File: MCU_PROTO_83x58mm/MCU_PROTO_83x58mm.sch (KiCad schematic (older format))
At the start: 15 parts, among them J1 Screw_Terminal_01x03, J10 Conn_01x01_Male, J2 Screw_Terminal_01x03, J3 Conn_01x20_Female, J4 Conn_01x20_Female, J5 Conn_01x20_Female, J6 Conn_01x20_Female, J7 Conn_01x20_Female, J8 Conn_01x20_Female, J9 Conn_01x01_Male

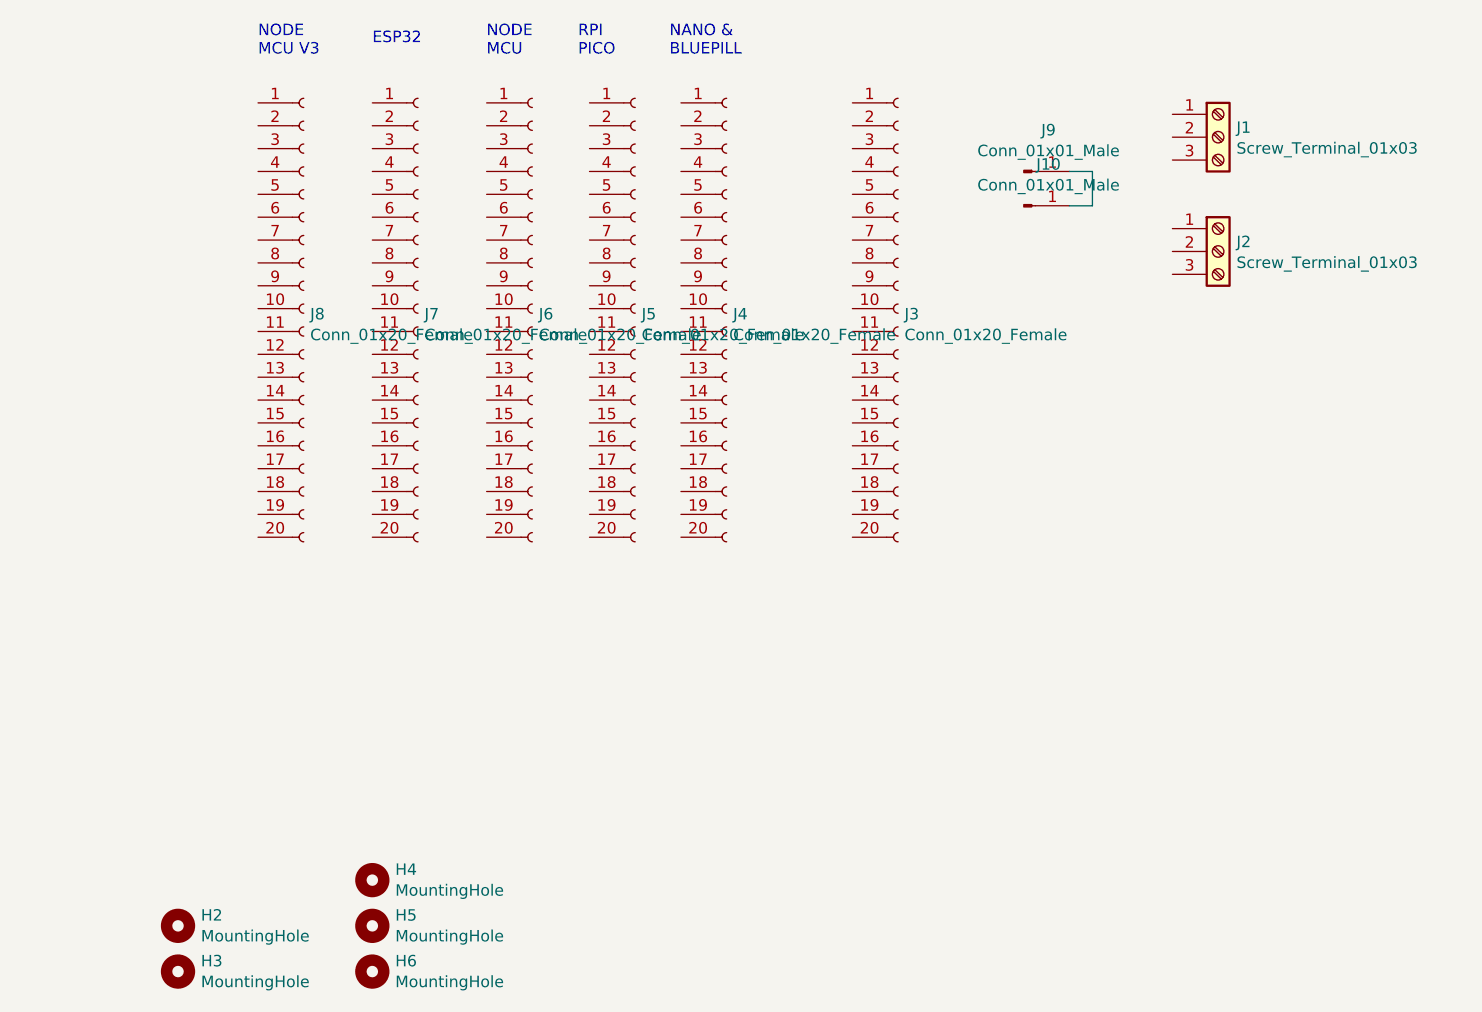
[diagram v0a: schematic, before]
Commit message: added rpi zero compat started
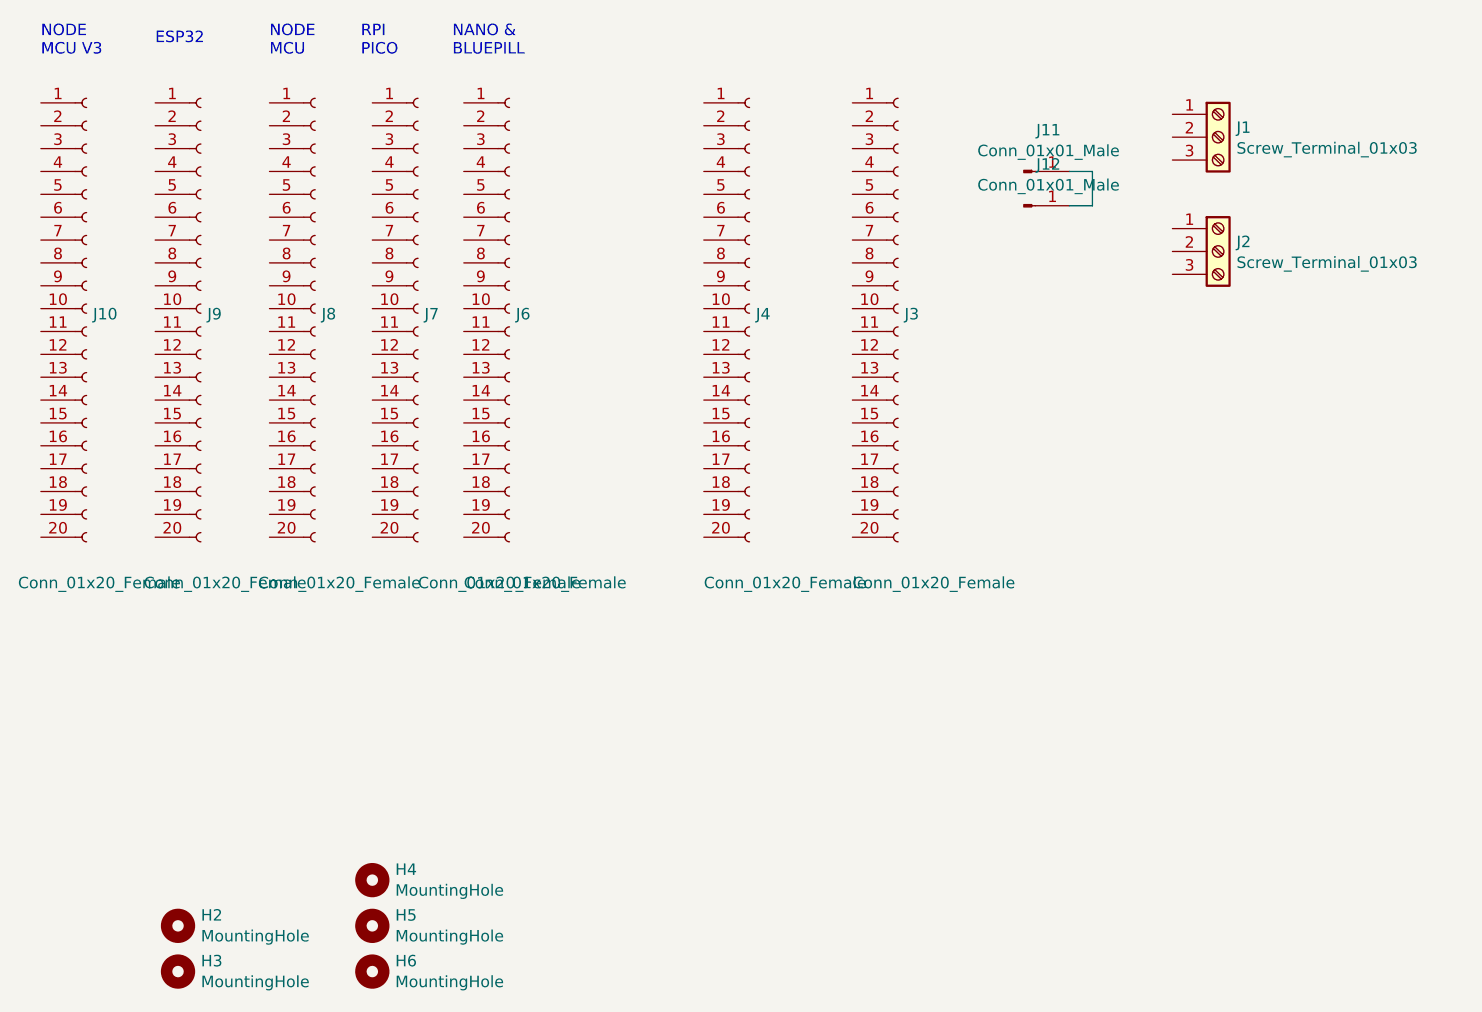
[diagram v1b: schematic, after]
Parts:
- added J4: Conn_01x20_Female, Connector_PinSocket_2.54mm:PinSocket_1x20_P2.54mm_Vertical, symbol Connector:Conn_01x20_Female
- renumbered J8 to J10, J9 to J11, J10 to J12, J4 to J6, J5 to J7, J6 to J8, J7 to J9
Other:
- moved on the sheet: J10, J6, J7, J8, J9
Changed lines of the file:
@@
 $EndComp
 $Comp
-L Connector:Conn_01x01_Male J9
+L Connector:Conn_01x01_Male J11
 U 1 1 6192FB40
 P 7300 1950
-F 0 "J9" H 7408 2131 50  0000 C CNN
+F 0 "J11" H 7408 2131 50  0000 C CNN
 F 1 "Conn_01x01_Male" H 7408 2040 50  0000 C CNN
 F 2 "Connector_Wire:SolderWirePad_1x01_Drill0.8mm" H 7300 1950 50  0001 C CNN
@@
 $EndComp
 $Comp
-L Connector:Conn_01x01_Male J10
+L Connector:Conn_01x01_Male J12
 U 1 1 61938D6F
 P 7300 2100
-F 0 "J10" H 7408 2281 50  0000 C CNN
+F 0 "J12" H 7408 2281 50  0000 C CNN
 F 1 "Conn_01x01_Male" H 7408 2190 50  0000 C CNN
 F 2 "Connector_Wire:SolderWirePad_1x01_Drill0.8mm" H 7300 2100 50  0001 C CNN
@@
 	7600 2100 7500 2100
 $Comp
-L Connector:Conn_01x20_Female J5
+L Connector:Conn_01x20_Female J7
 U 1 1 619361D7
-P 5600 2550
-F 0 "J5" H 5628 2526 50  0000 L CNN
-F 1 "Conn_01x20_Female" H 5628 2435 50  0000 L CNN
-F 2 "Connector_PinSocket_2.54mm:PinSocket_1x20_P2.54mm_Vertical" H 5600 2550 50  0001 C CNN
-F 3 "~" H 5600 2550 50  0001 C CNN
-	1    5600 2550
+P 4650 2550
+F 0 "J7" H 4678 2526 50  0000 L CNN
+F 1 "Conn_01x20_Female" H 4650 1350 50  0000 L CNN
+F 2 "Connector_PinSocket_2.54mm:PinSocket_1x20_P2.54mm_Vertical" H 4650 2550 50  0001 C CNN
+F 3 "~" H 4650 2550 50  0001 C CNN
+	1    4650 2550
 	1    0    0    -1
 $EndComp
@@
 P 6750 2550
 F 0 "J3" H 6778 2526 50  0000 L CNN
-F 1 "Conn_01x20_Female" H 6778 2435 50  0000 L CNN
+F 1 "Conn_01x20_Female" H 6550 1350 50  0000 L CNN
 F 2 "Connector_PinSocket_2.54mm:PinSocket_1x20_P2.54mm_Vertical" H 6750 2550 50  0001 C CNN
 F 3 "~" H 6750 2550 50  0001 C CNN
@@
 	1    0    0    -1
 $EndComp
-Text Notes 5750 1450 0    50   ~ 0
+Text Notes 4800 1450 0    50   ~ 0
 NANO &\nBLUEPILL
 $Comp
-L Connector:Conn_01x20_Female J4
+L Connector:Conn_01x20_Female J6
 U 1 1 61975404
-P 6000 2550
-F 0 "J4" H 6028 2526 50  0000 L CNN
-F 1 "Conn_01x20_Female" H 6028 2435 50  0000 L CNN
-F 2 "Connector_PinSocket_2.54mm:PinSocket_1x20_P2.54mm_Vertical" H 6000 2550 50  0001 C CNN
-F 3 "~" H 6000 2550 50  0001 C CNN
-	1    6000 2550
+P 5050 2550
+F 0 "J6" H 5078 2526 50  0000 L CNN
+F 1 "Conn_01x20_Female" H 4850 1350 50  0000 L CNN
+F 2 "Connector_PinSocket_2.54mm:PinSocket_1x20_P2.54mm_Vertical" H 5050 2550 50  0001 C CNN
+F 3 "~" H 5050 2550 50  0001 C CNN
+	1    5050 2550
 	1    0    0    -1
 $EndComp
-Text Notes 5350 1450 0    50   ~ 0
+Text Notes 4400 1450 0    50   ~ 0
 RPI\nPICO
 $Comp
-L Connector:Conn_01x20_Female J6
+L Connector:Conn_01x20_Female J8
 U 1 1 6199B975
-P 5150 2550
-F 0 "J6" H 5178 2526 50  0000 L CNN
-F 1 "Conn_01x20_Female" H 5178 2435 50  0000 L CNN
-F 2 "Connector_PinSocket_2.54mm:PinSocket_1x20_P2.54mm_Vertical" H 5150 2550 50  0001 C CNN
-F 3 "~" H 5150 2550 50  0001 C CNN
-	1    5150 2550
+P 4200 2550
+F 0 "J8" H 4228 2526 50  0000 L CNN
+F 1 "Conn_01x20_Female" H 3950 1350 50  0000 L CNN
+F 2 "Connector_PinSocket_2.54mm:PinSocket_1x20_P2.54mm_Vertical" H 4200 2550 50  0001 C CNN
+F 3 "~" H 4200 2550 50  0001 C CNN
+	1    4200 2550
 	1    0    0    -1
 $EndComp
-Text Notes 4950 1450 0    50   ~ 0
+Text Notes 4000 1450 0    50   ~ 0
 NODE\nMCU
 $Comp
-L Connector:Conn_01x20_Female J7
+L Connector:Conn_01x20_Female J9
 U 1 1 619B2BAA
-P 4650 2550
-F 0 "J7" H 4678 2526 50  0000 L CNN
-F 1 "Conn_01x20_Female" H 4678 2435 50  0000 L CNN
-F 2 "Connector_PinSocket_2.54mm:PinSocket_1x20_P2.54mm_Vertical" H 4650 2550 50  0001 C CNN
-F 3 "~" H 4650 2550 50  0001 C CNN
-	1    4650 2550
+P 3700 2550
+F 0 "J9" H 3728 2526 50  0000 L CNN
+F 1 "Conn_01x20_Female" H 3450 1350 50  0000 L CNN
+F 2 "Connector_PinSocket_2.54mm:PinSocket_1x20_P2.54mm_Vertical" H 3700 2550 50  0001 C CNN
+F 3 "~" H 3700 2550 50  0001 C CNN
+	1    3700 2550
 	1    0    0    -1
 $EndComp
-Text Notes 4450 1400 0    50   ~ 0
+Text Notes 3500 1400 0    50   ~ 0
 ESP32
 $Comp
-L Connector:Conn_01x20_Female J8
+L Connector:Conn_01x20_Female J10
 U 1 1 619DA776
-P 4150 2550
-F 0 "J8" H 4178 2526 50  0000 L CNN
-F 1 "Conn_01x20_Female" H 4178 2435 50  0000 L CNN
-F 2 "Connector_PinSocket_2.54mm:PinSocket_1x20_P2.54mm_Vertical" H 4150 2550 50  0001 C CNN
-F 3 "~" H 4150 2550 50  0001 C CNN
-	1    4150 2550
+P 3200 2550
+F 0 "J10" H 3228 2526 50  0000 L CNN
+F 1 "Conn_01x20_Female" H 2900 1350 50  0000 L CNN
+F 2 "Connector_PinSocket_2.54mm:PinSocket_1x20_P2.54mm_Vertical" H 3200 2550 50  0001 C CNN
+F 3 "~" H 3200 2550 50  0001 C CNN
+	1    3200 2550
 	1    0    0    -1
 $EndComp
-Text Notes 3950 1450 0    50   ~ 0
+Text Notes 3000 1450 0    50   ~ 0
 NODE\nMCU V3
 $Comp
@@
 	1    0    0    -1
 $EndComp
+$Comp
+L Connector:Conn_01x20_Female J4
+U 1 1 6217E1D9
+P 6100 2550
+F 0 "J4" H 6128 2526 50  0000 L CNN
+F 1 "Conn_01x20_Female" H 5900 1350 50  0000 L CNN
+F 2 "Connector_PinSocket_2.54mm:PinSocket_1x20_P2.54mm_Vertical" H 6100 2550 50  0001 C CNN
+F 3 "~" H 6100 2550 50  0001 C CNN
+	1    6100 2550
+	1    0    0    -1
+$EndComp

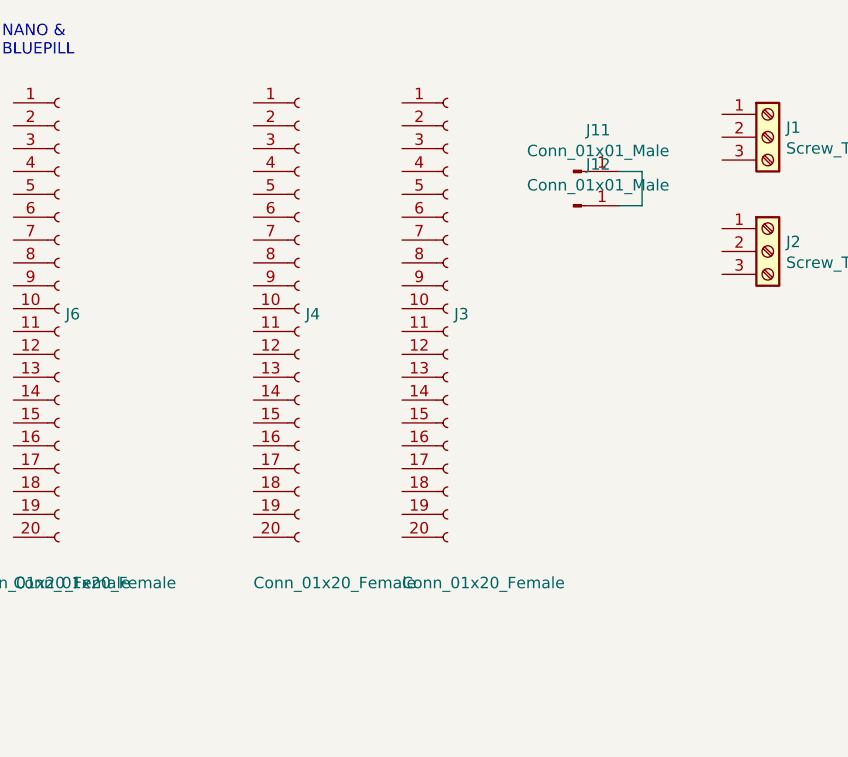
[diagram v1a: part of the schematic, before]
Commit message: pi zero added single gerber
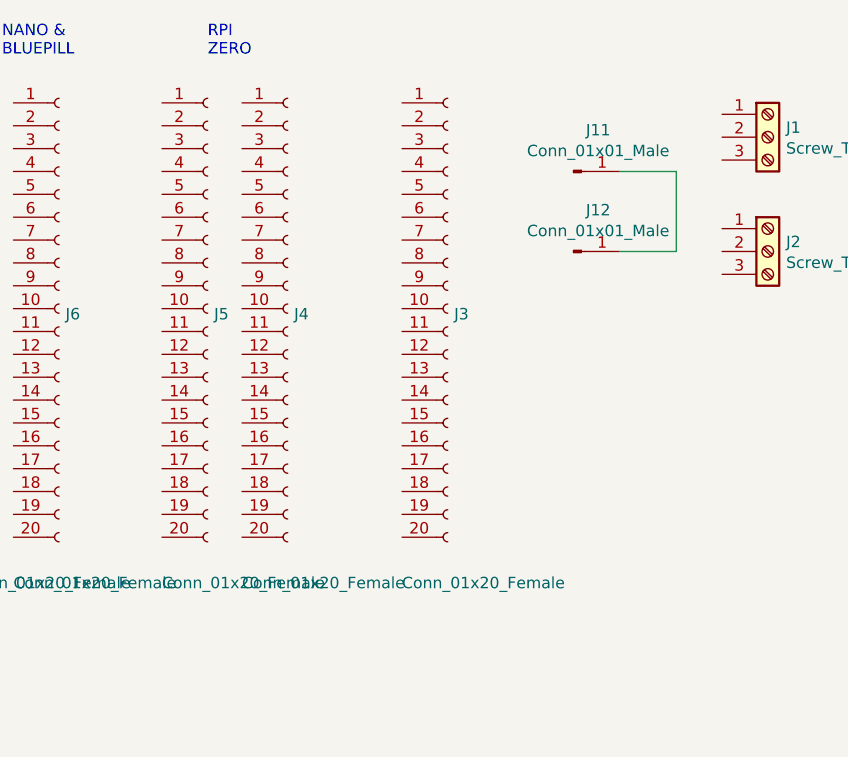
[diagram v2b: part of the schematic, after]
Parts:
- added J5: Conn_01x20_Female, Connector_PinSocket_2.54mm:PinSocket_1x20_P2.54mm_Vertical, symbol Connector:Conn_01x20_Female
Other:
- note added: "RPI\nZERO"
- moved on the sheet: J12, J4
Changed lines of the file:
@@
 L Connector:Conn_01x01_Male J12
 U 1 1 61938D6F
-P 7300 2100
-F 0 "J12" H 7408 2281 50  0000 C CNN
-F 1 "Conn_01x01_Male" H 7408 2190 50  0000 C CNN
-F 2 "Connector_Wire:SolderWirePad_1x01_Drill0.8mm" H 7300 2100 50  0001 C CNN
-F 3 "~" H 7300 2100 50  0001 C CNN
-	1    7300 2100
+P 7300 2300
+F 0 "J12" H 7408 2481 50  0000 C CNN
+F 1 "Conn_01x01_Male" H 7408 2390 50  0000 C CNN
+F 2 "Connector_Wire:SolderWirePad_1x01_Drill0.8mm" H 7300 2300 50  0001 C CNN
+F 3 "~" H 7300 2300 50  0001 C CNN
+	1    7300 2300
 	1    0    0    -1
 $EndComp
-Wire Wire Line
-	7500 1950 7600 1950
-Wire Wire Line
-	7600 1950 7600 2100
-Wire Wire Line
-	7600 2100 7500 2100
 $Comp
 L Connector:Conn_01x20_Female J7
@@
 L Connector:Conn_01x20_Female J4
 U 1 1 6217E1D9
-P 6100 2550
-F 0 "J4" H 6128 2526 50  0000 L CNN
-F 1 "Conn_01x20_Female" H 5900 1350 50  0000 L CNN
-F 2 "Connector_PinSocket_2.54mm:PinSocket_1x20_P2.54mm_Vertical" H 6100 2550 50  0001 C CNN
-F 3 "~" H 6100 2550 50  0001 C CNN
-	1    6100 2550
+P 6050 2550
+F 0 "J4" H 6078 2526 50  0000 L CNN
+F 1 "Conn_01x20_Female" H 5850 1350 50  0000 L CNN
+F 2 "Connector_PinSocket_2.54mm:PinSocket_1x20_P2.54mm_Vertical" H 6050 2550 50  0001 C CNN
+F 3 "~" H 6050 2550 50  0001 C CNN
+	1    6050 2550
 	1    0    0    -1
 $EndComp
+$Comp
+L Connector:Conn_01x20_Female J5
+U 1 1 620C51CD
+P 5700 2550
+F 0 "J5" H 5728 2526 50  0000 L CNN
+F 1 "Conn_01x20_Female" H 5500 1350 50  0000 L CNN
+F 2 "Connector_PinSocket_2.54mm:PinSocket_1x20_P2.54mm_Vertical" H 5700 2550 50  0001 C CNN
+F 3 "~" H 5700 2550 50  0001 C CNN
+	1    5700 2550
+	1    0    0    -1
+$EndComp
+Wire Wire Line
+	7500 1950 7750 1950
+Wire Wire Line
+	7750 1950 7750 2300
+Wire Wire Line
+	7750 2300 7500 2300
+Text Notes 5700 1450 0    50   ~ 0
+RPI\nZERO
 $EndSCHEMATC

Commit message: gerbers sinlge corrected
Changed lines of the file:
@@
 Text Notes 4800 1450 0    50   ~ 0
 NANO &\nBLUEPILL
-$Comp
-L Connector:Conn_01x20_Female J6
-U 1 1 61975404
-P 5050 2550
-F 0 "J6" H 5078 2526 50  0000 L CNN
-F 1 "Conn_01x20_Female" H 4850 1350 50  0000 L CNN
-F 2 "Connector_PinSocket_2.54mm:PinSocket_1x20_P2.54mm_Vertical" H 5050 2550 50  0001 C CNN
-F 3 "~" H 5050 2550 50  0001 C CNN
-	1    5050 2550
-	1    0    0    -1
-$EndComp
 Text Notes 4400 1450 0    50   ~ 0
 RPI\nPICO
@@
 $EndComp
 $Comp
-L Connector:Conn_01x20_Female J4
-U 1 1 6217E1D9
-P 6050 2550
-F 0 "J4" H 6078 2526 50  0000 L CNN
-F 1 "Conn_01x20_Female" H 5850 1350 50  0000 L CNN
-F 2 "Connector_PinSocket_2.54mm:PinSocket_1x20_P2.54mm_Vertical" H 6050 2550 50  0001 C CNN
-F 3 "~" H 6050 2550 50  0001 C CNN
-	1    6050 2550
-	1    0    0    -1
-$EndComp
-$Comp
 L Connector:Conn_01x20_Female J5
 U 1 1 620C51CD
@@
 Text Notes 5700 1450 0    50   ~ 0
 RPI\nZERO
+$Comp
+L Connector:Conn_01x20_Female J6
+U 1 1 620D8961
+P 5050 2550
+F 0 "J6" H 5078 2526 50  0000 L CNN
+F 1 "Conn_01x20_Female" H 5078 2435 50  0000 L CNN
+F 2 "Connector_PinSocket_2.54mm:PinSocket_1x20_P2.54mm_Vertical" H 5050 2550 50  0001 C CNN
+F 3 "~" H 5050 2550 50  0001 C CNN
+	1    5050 2550
+	1    0    0    -1
+$EndComp
+$Comp
+L Connector:Conn_01x20_Female J4
+U 1 1 620DD7F6
+P 6050 2550
+F 0 "J4" H 6078 2526 50  0000 L CNN
+F 1 "Conn_01x20_Female" H 6078 2435 50  0000 L CNN
+F 2 "Connector_PinSocket_2.54mm:PinSocket_1x20_P2.54mm_Vertical" H 6050 2550 50  0001 C CNN
+F 3 "~" H 6050 2550 50  0001 C CNN
+	1    6050 2550
+	1    0    0    -1
+$EndComp
 $EndSCHEMATC
